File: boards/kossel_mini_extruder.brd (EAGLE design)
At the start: 66.9 x 57.9 mm, 31 parts

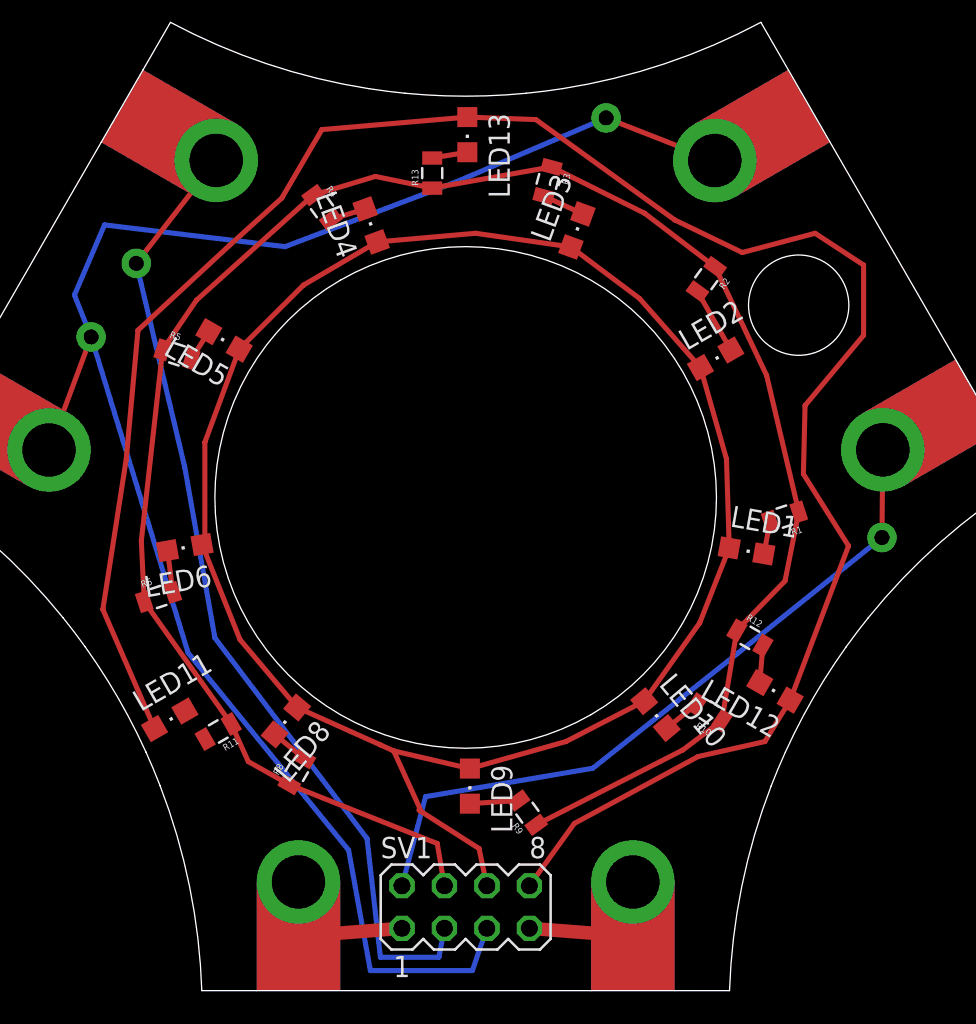
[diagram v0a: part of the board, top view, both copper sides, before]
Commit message: moved red leds onto hot end circuit
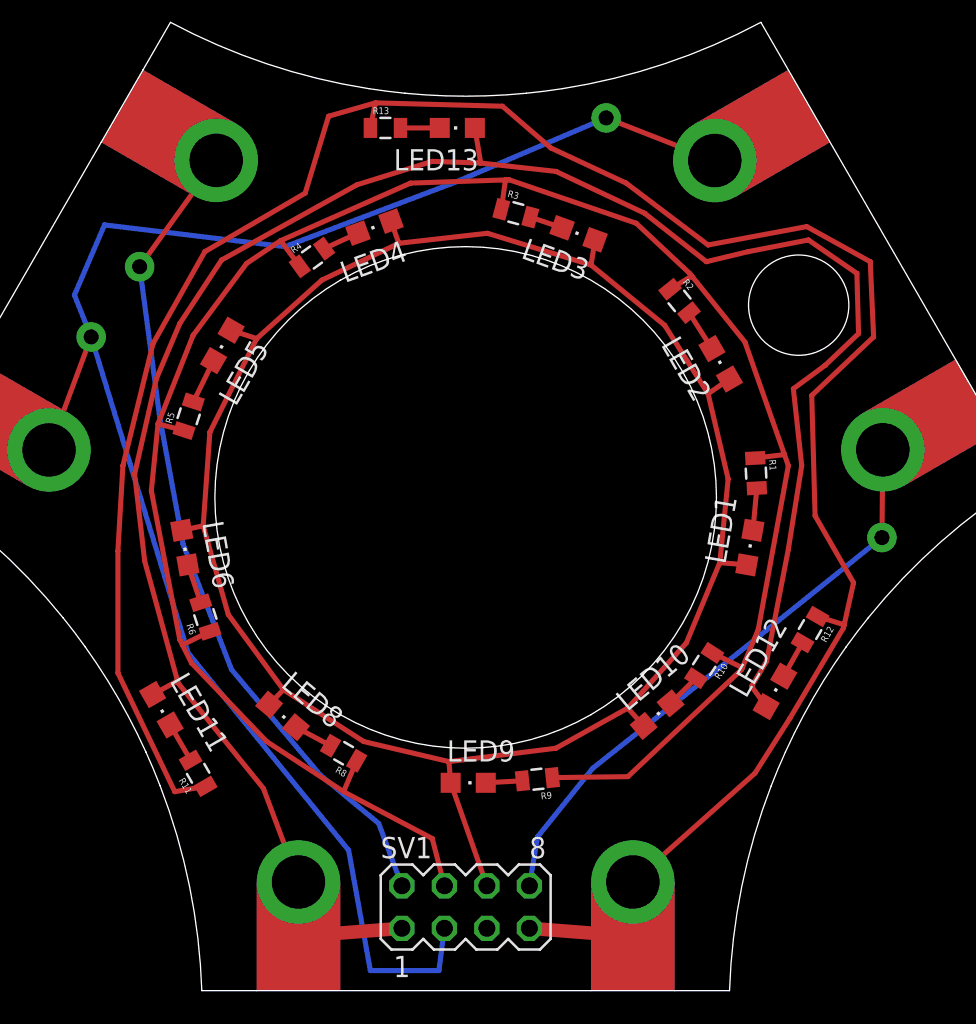
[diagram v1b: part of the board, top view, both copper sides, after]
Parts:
- moved R13 3.89 mm to (28.2, 51.1), turned to 0 degrees
- moved R5 3.77 mm to (16.4, 33.9), turned to 72 degrees
- moved R12 3.63 mm to (53.6, 21.1), turned to 240 degrees
- moved R1 3.11 mm to (50.4, 30.5), turned to 273 degrees
- moved R4 3.06 mm to (23.8, 43.4), turned to 36 degrees
- moved R6 3.05 mm to (17.4, 21.8), turned to 108 degrees
- moved R8 3.01 mm to (25.7, 13.7), turned to 150 degrees
- moved R10 2.82 mm to (47.3, 18.9), turned to 237 degrees
- moved R11 2.77 mm to (17.0, 12.5), turned to 120 degrees
- moved R3 2.69 mm to (36.0, 46.0), turned to 345 degrees
- moved R9 2.09 mm to (37.3, 12.1), turned to 186 degrees
- moved R2 2.06 mm to (45.8, 40.8), turned to 309 degrees
- moved LED11 0.78 mm to (14.8, 16.3), turned to 300 degrees
- moved LED13 0.72 mm to (32.5, 51.1), turned to 180 degrees
- moved LED2 0.42 mm to (48.3, 37.0), turned to 120 degrees
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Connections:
- removed net N$11: SV1.3, THERM_SIG.P$1, THERM_SIG.P$2, THERM_SIG.P$3
- removed net N$15: HOT_PWM.P$1, HOT_PWM.P$2, HOT_PWM.P$3, SV1.7
- new net N$7: HOT_PWM.P$1, HOT_PWM.P$2, HOT_PWM.P$3, R11.1, R12.1, R13.1, SV1.7
- net GND: no longer R11.1, R12.1, R13.1
- net N$10: now also SV1.2, THERM_SIG.P$1, THERM_SIG.P$2, THERM_SIG.P$3; no longer HOT_12V.P$1, HOT_12V.P$2, HOT_12V.P$3, SV1.1
- net N$20: now also SV1.8; no longer SV1.2
- net N$8: now also SV1.3; no longer SV1.5
- net VCC1: now also HOT_12V.P$1, HOT_12V.P$2, HOT_12V.P$3, SV1.1; no longer SV1.8
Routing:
- net N$7: track 0.00 -> 140.3 mm
- net N$11: track 61.4 -> 0.00 mm, vias 1 -> 0
- net N$10: track 9.46 -> 52.7 mm, vias 0 -> 1
- net N$15: track 9.46 -> 0.00 mm
- net VCC: track 110.2 -> 118.2 mm
- net N$20: track 46.3 -> 38.9 mm
- net GND: track 122.7 -> 129.8 mm
- net N$16: track 0.00 -> 2.44 mm
- net N$8: track 110.6 -> 108.5 mm
- net N$2: track 4.04 -> 2.55 mm
- net VCC1: track 125.3 -> 124.4 mm
- net N$5: track 1.95 -> 2.75 mm
- net N$13: track 2.92 -> 2.20 mm
- net N$3: track 2.58 -> 2.00 mm
- net N$1: track 1.99 -> 2.53 mm

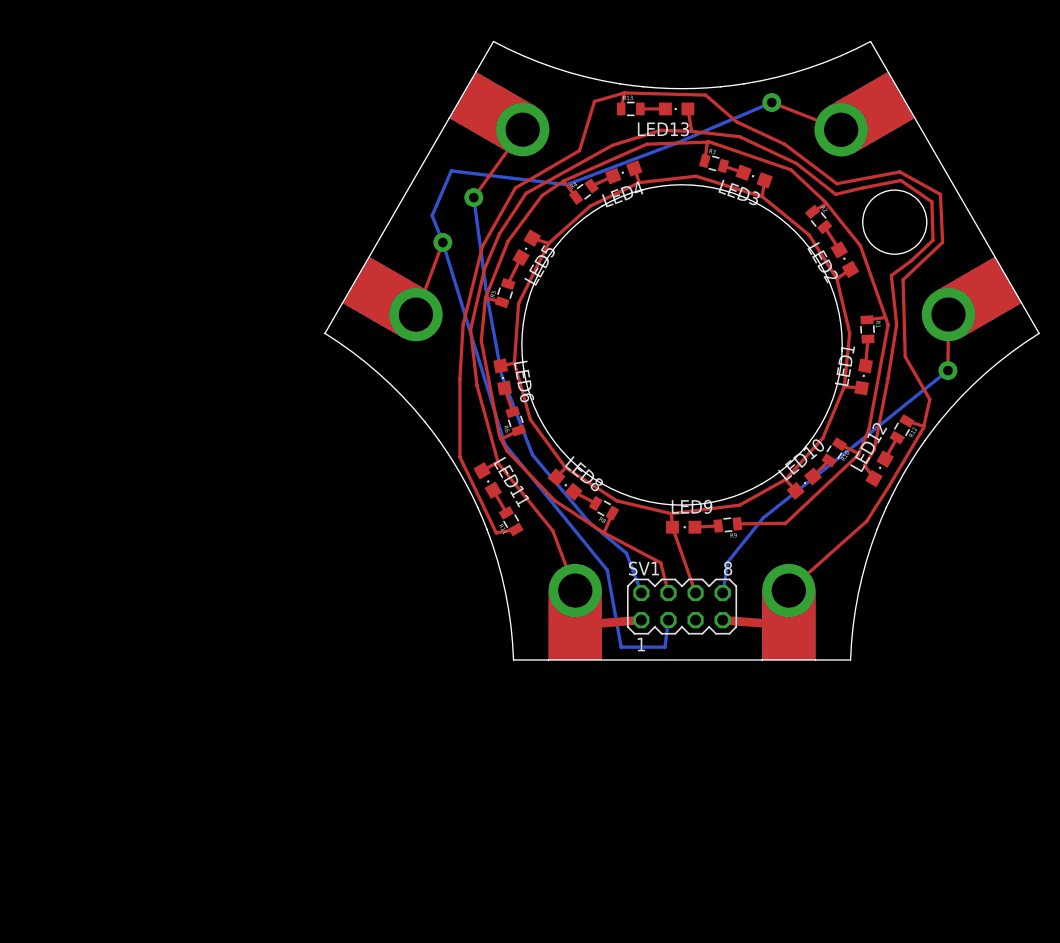
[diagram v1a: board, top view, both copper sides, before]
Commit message: started rev of end effector board
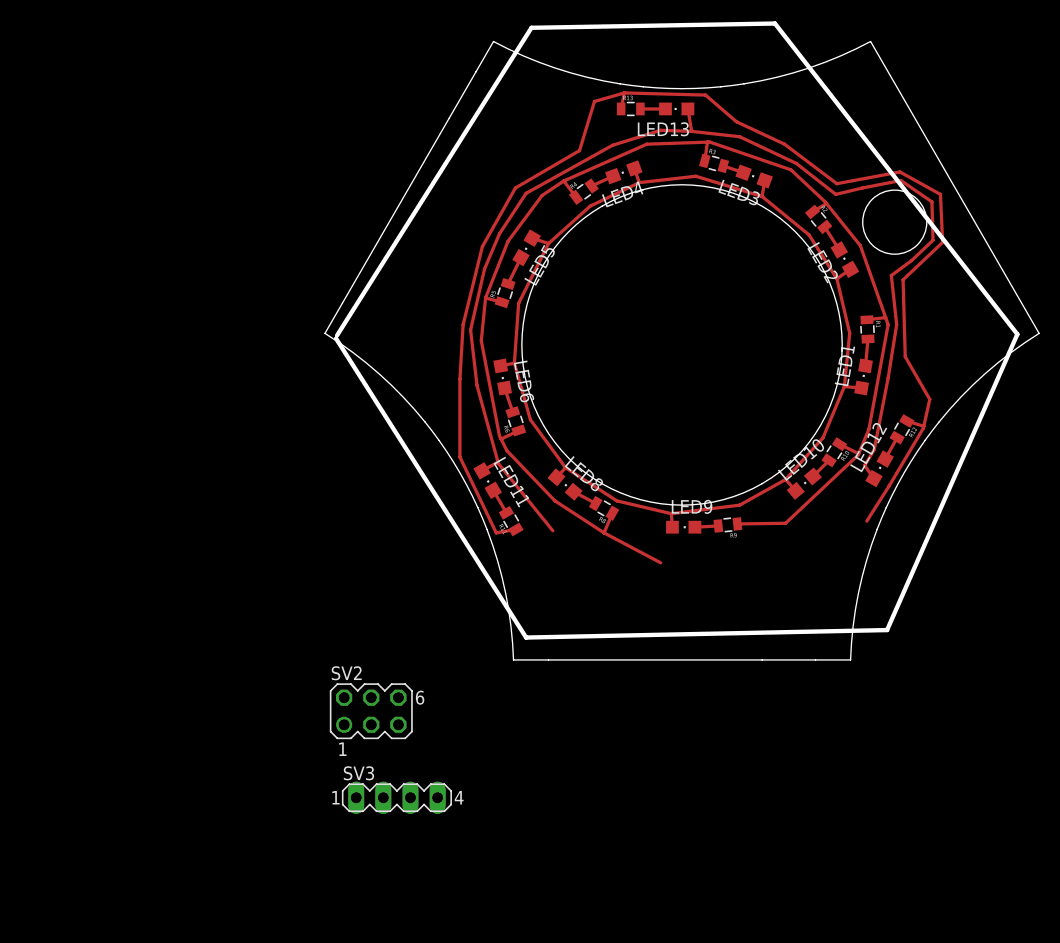
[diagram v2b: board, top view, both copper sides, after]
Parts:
- removed HOT_12V, HOT_PWM, PROBE_GND, PROBE_SIG, THERM_GND, THERM_SIG: LUG3-X, OBKP_Effector_PCB:3MM
- removed SV1: (no value), con-lstb:MA04-2
- added SV2: (no value), con-lstb:MA03-2
- added SV3: (no value), con-lstb:MA04-1
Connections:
- removed net N$10: SV1.2, THERM_SIG.P$1, THERM_SIG.P$2, THERM_SIG.P$3
- removed net N$20: PROBE_SIG.P$1, PROBE_SIG.P$2, PROBE_SIG.P$3, SV1.8
- removed net N$7: HOT_PWM.P$1, HOT_PWM.P$2, HOT_PWM.P$3, R11.1, R12.1, R13.1, SV1.7
- removed net N$8: PROBE_GND.P$1, PROBE_GND.P$2, PROBE_GND.P$3, SV1.3, THERM_GND.P$1, THERM_GND.P$2, THERM_GND.P$3
- removed net VCC1: HOT_12V.P$1, HOT_12V.P$2, HOT_12V.P$3, LED11.A, LED12.A, LED13.A, SV1.1
- new net HOT_12V: R11.1, R12.1, R13.1, SV2.5, SV3.1
- new net HOT_SIG: LED11.A, LED12.A, LED13.A, SV2.1, SV3.2
- new net THERM_GND: SV2.3, SV3.4
- new net THERM_SIG: SV2.2, SV3.3
- net GND: now also SV2.4; no longer SV1.4
- net VCC: now also SV2.6; no longer SV1.6
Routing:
- net N$7: track 140.3 -> 0.00 mm
- net VCC1: track 124.4 -> 0.00 mm
- net HOT_12V: track 0.00 -> 121.1 mm
- net HOT_SIG: track 0.00 -> 108.9 mm
- net N$8: track 108.5 -> 0.00 mm, vias 2 -> 0
- net N$10: track 52.7 -> 0.00 mm, vias 1 -> 0
- net N$20: track 38.9 -> 0.00 mm, vias 1 -> 0
- net VCC: track 118.2 -> 111.7 mm
- net GND: track 129.8 -> 126.9 mm
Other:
- board size 66.9 x 57.9 mm -> 66.9 x 59.6 mm

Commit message: grinding on effector board
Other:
- board size 66.9 x 59.6 mm -> 76.9 x 69 mm
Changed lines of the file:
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@@
 <?xml version="1.0" encoding="utf-8"?>
 <!DOCTYPE eagle SYSTEM "eagle.dtd">
-<eagle version="6.4">
+<eagle version="6.5.0">
 <drawing>
 <settings>
@@
 <board>
 <plain>
-<wire x1="13.703215625" y1="54.57500625" x2="15.343096875" y2="57.41665" width="0" layer="20"/>
-<wire x1="15.343096875" y1="57.41665" x2="27.195490625" y2="53.4514875" width="0" layer="20" curve="19.185143"/>
-<wire x1="29.371096875" y1="53.17544375" x2="36.62945" y2="53.175440625" width="0" layer="20" curve="11.107305"/>
-<wire x1="38.805896875" y1="53.451878125" x2="50.6572875" y2="57.416665625" width="0" layer="20" curve="19.183513"/>
-<wire x1="50.65724375" y1="57.41674375" x2="66.43874375" y2="30.082384375" width="0" layer="20"/>
-<wire x1="66.43874375" y1="30.082384375" x2="57.079340625" y2="21.801296875" width="0" layer="20" curve="19.183565"/>
-<wire x1="55.75193125" y1="20.05449375" x2="52.122771875" y2="13.76860625" width="0" layer="20" curve="11.107307"/>
-<wire x1="51.274015625" y1="11.746471875" x2="48.781875" y2="-0.500528125" width="0" layer="20" curve="19.18495"/>
-<wire x1="48.78159375" y1="-0.50051875" x2="45.500715625" y2="-0.49986875" width="0" layer="20"/>
-<wire x1="40.49995625" y1="-0.500309375" x2="20.5004" y2="-0.50005625" width="0" layer="20"/>
-<wire x1="20.5004" y1="-0.50005625" x2="17.21865625" y2="-0.49990625" width="0" layer="20"/>
-<wire x1="17.21865625" y1="-0.49990625" x2="14.72683125" y2="11.745809375" width="0" layer="20" curve="19.182953"/>
-<wire x1="13.877971875" y1="13.768328125" x2="10.248471875" y2="20.05480625" width="0" layer="20" curve="11.108308"/>
-<wire x1="8.921446875" y1="21.801278125" x2="-0.4384375" y2="30.082753125" width="0" layer="20" curve="19.184384"/>
-<wire x1="-0.4383375" y1="30.082909375" x2="1.202903125" y2="32.92419375" width="0" layer="20"/>
-<wire x1="1.202903125" y1="32.92419375" x2="11.202459375" y2="50.244440625" width="0" layer="20"/>
-<wire x1="11.202459375" y1="50.244440625" x2="13.703215625" y2="54.57500625" width="0" layer="20"/>
-<wire x1="27.195515625" y1="53.451659375" x2="29.371115625" y2="53.1756625" width="0" layer="20" curve="3.351177"/>
-<wire x1="36.62943125" y1="53.1756375" x2="38.805921875" y2="53.45174375" width="0" layer="20" curve="3.352571"/>
-<wire x1="10.248471875" y1="20.05480625" x2="8.92140625" y2="21.80124375" width="0" layer="20" curve="3.351788"/>
-<wire x1="14.726946875" y1="11.74585625" x2="13.87801875" y2="13.76835" width="0" layer="20" curve="3.351789"/>
-<wire x1="57.0794" y1="21.80125" x2="55.7520625" y2="20.054396875" width="0" layer="20" curve="3.352554"/>
-<wire x1="52.122596875" y1="13.7686875" x2="51.2737875" y2="11.7465625" width="0" layer="20" curve="3.351205"/>
-<wire x1="45.500715625" y1="-0.49986875" x2="40.49995625" y2="-0.500309375" width="0" layer="20"/>
 <wire x1="25.5" y1="41.990378125" x2="40.5" y2="16.00961875" width="0" layer="20" curve="180"/>
 <wire x1="25.5" y1="41.990378125" x2="40.5" y2="16.00961875" width="0" layer="20" curve="-180"/>
-<hole x="52.91858125" y="40.5" drill="6"/>
-<wire x1="0.7" y1="29.9" x2="18.9" y2="58.7" width="0.4064" layer="20"/>
-<wire x1="18.9" y1="58.7" x2="41.7" y2="59.1" width="0.4064" layer="20"/>
-<wire x1="41.7" y1="59.1" x2="64.4" y2="30" width="0.4064" layer="20"/>
-<wire x1="64.4" y1="30" x2="52.2" y2="2.3" width="0.4064" layer="20"/>
-<wire x1="52.2" y1="2.3" x2="18.4" y2="1.6" width="0.4064" layer="20"/>
-<wire x1="18.4" y1="1.6" x2="0.6" y2="29.6" width="0.4064" layer="20"/>
+<wire x1="28.87" y1="0" x2="14.43" y2="25" width="0" layer="20"/>
+<wire x1="14.43" y1="25" x2="-14.43" y2="25" width="0" layer="20"/>
+<wire x1="-14.43" y1="25" x2="-28.87" y2="0" width="0" layer="20"/>
+<wire x1="-28.87" y1="0" x2="-14.43" y2="-25" width="0" layer="20"/>
+<wire x1="-14.43" y1="-25" x2="14.43" y2="-25" width="0" layer="20"/>
+<wire x1="14.43" y1="-25" x2="28.87" y2="0" width="0" layer="20"/>
+<circle x="0" y="0" radius="13.1" width="0.1" layer="20"/>
 </plain>
 <attributes>

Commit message: still grinding on board
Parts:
- removed LED10, LED8, LED9: (no value), SparkFun-LED:CHIPLED_0805
- removed R10, R8, R9: (no value), SparkFun-Passives:0805
- moved SV3 54.4 mm to (11.2, 40.8), turned to 240 degrees
- moved SV2 29.8 mm to (30.0, 9.00)
- moved R1 19.9 mm to (39.7, 13.7), turned to 120 degrees
- moved LED1 15.1 mm to (37.6, 17.3), turned to 300 degrees
- moved R2 11.9 mm to (48.9, 29.3), turned to 180 degrees
- moved LED6 10.7 mm to (22.4, 17.3), turned to 240 degrees
- moved LED5 9.34 mm to (15.0, 29.4), turned to 180 degrees
- moved R6 8.95 mm to (20.2, 13.3), turned to 60 degrees
- moved LED2 8.77 mm to (44.1, 29.3), turned to 0 degrees
- moved R5 7.58 mm to (10.3, 29.4), turned to 0 degrees
- moved LED4 6.04 mm to (22.2, 42.3), turned to 120 degrees
- moved LED11 5.57 mm to (9.60, 18.3)
- moved R4 5.26 mm to (19.7, 46.7), turned to 300 degrees
- moved R11 5.07 mm to (12.1, 13.8)
- moved R3 4.37 mm to (40.2, 44.8), turned to 240 degrees
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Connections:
- removed net N$13: LED9.C, R9.2
- removed net N$14: LED10.C, R10.2
- removed net N$9: LED8.C, R8.2
- net GND: no longer R10.1, R8.1, R9.1
- net VCC: no longer LED10.A, LED8.A, LED9.A
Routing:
- net GND: track 126.9 -> 0.00 mm
- net HOT_12V: track 121.1 -> 0.00 mm
- net VCC: track 111.7 -> 0.00 mm
- net HOT_SIG: track 108.9 -> 0.00 mm
- net N$5: track 2.75 -> 0.00 mm
- net N$2: track 2.55 -> 0.00 mm
- net N$1: track 2.53 -> 0.00 mm
- net N$16: track 2.44 -> 0.00 mm
- net N$6: track 2.39 -> 0.00 mm
- net N$18: track 2.35 -> 0.00 mm
- net N$9: track 2.35 -> 0.00 mm
- net N$17: track 2.30 -> 0.00 mm
- net N$4: track 2.23 -> 0.00 mm
- net N$13: track 2.20 -> 0.00 mm
- net N$14: track 2.14 -> 0.00 mm
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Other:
- board size 76.9 x 69 mm -> 57.7 x 50 mm
